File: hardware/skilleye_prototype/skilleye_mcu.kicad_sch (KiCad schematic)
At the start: 11 parts, among them SW1 SW_Push_45deg, SW2 SW_Push, U4 ESP32-C6-WROOM-1 (N8), U5 LSM6DS0

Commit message: added MCU schematic + datasheets
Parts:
- removed SW2: SW_Push, symbol Switch:SW_Push
- added C10: 0.1uF, symbol Device:C_Small
- added R10: 10K, symbol Device:R_Small
- added SW2: SW_Push_45deg, symbol Switch:SW_Push_45deg
- added TP1, TP2, TP3, TP4, TP5: TestPoint_Flag, symbol Connector:TestPoint_Flag
- C6: value 10uF -> 22uF
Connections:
- net +3V3: now also C9.1, R8.2, R9.2, U5.5 (VDDIO), U5.8 (VDD), C10.1, R10.2
- net GND: now also C9.2, U5.2 (SDIX), U5.3 (SCX), U5.6 (GND@6), U5.7 (GND@7), C10.2, SW2.2
- net at U4.10 (GPIO8): now also R8.1
- net at U4.11 (GPIO10): now also TP5.1
- net USB_DM: now reaches U4.13 (GPIO12/USB_D-)
- net USB_DP: now reaches U4.14 (GPIO13/USB_D+)
- net at U4.15 (GPIO9): now also R9.1, SW2.1
- net SPI_MOSI: now reaches U4.16 (GPIO18)
- net SPI_MOSI: now also U5.14 (SDA)
- net SPI_CLK: now reaches U4.17 (GPIO19)
- net SPI_CLK: now also U5.13 (SCL)
- net SPI_CS: now reaches U4.18 (GPIO20)
- net SPI_CS: now also U5.12 (~{CS}), R10.1
- net SPI_MISO: now reaches U4.19 (GPIO21)
- net SPI_MISO: now also U5.1 (SDO/SA0)
- net IMU_INT1: now reaches U4.20 (GPIO22)
- net IMU_INT1: now also U5.4 (INT1)
- net IMU_INT2: now reaches U4.21 (GPIO23)
- net IMU_INT2: now also U5.9 (INT2)
- net at U4.24 (U0RXD/GPIO17): now also TP2.1
- net at U4.25 (U0TXD/GPIO16): now also TP1.1
- net at U4.26 (GPIO3/ADC1_CH3): now also TP4.1
- net at U4.27 (GPIO2/ADC1_CH2): now also TP3.1
- no-connect marks 0 -> 10
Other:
- title: (none) -> MCU
- moved on the sheet: C6, C7, C8, C9, R7, R8, R9, SW1, U4, U5

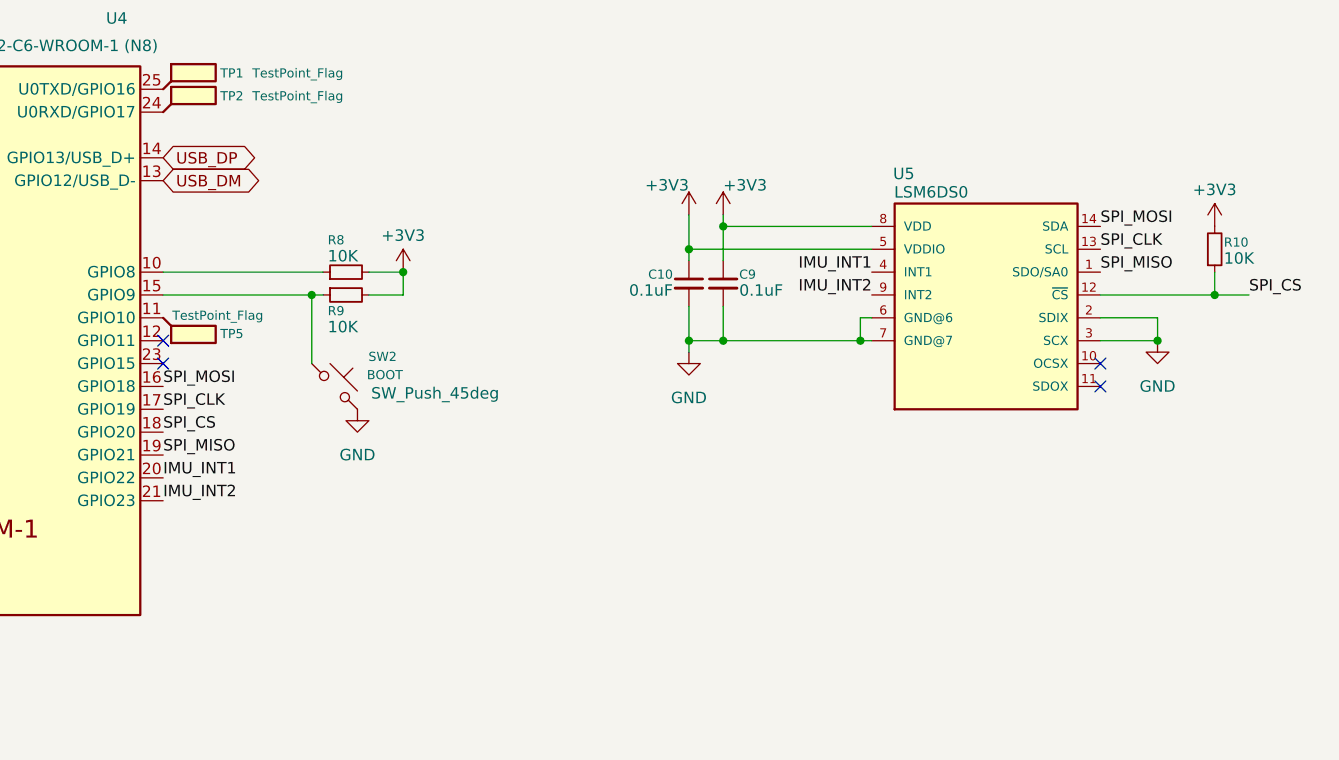
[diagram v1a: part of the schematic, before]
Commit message: prototype schematic rev1.1 - add VBUS sense divider
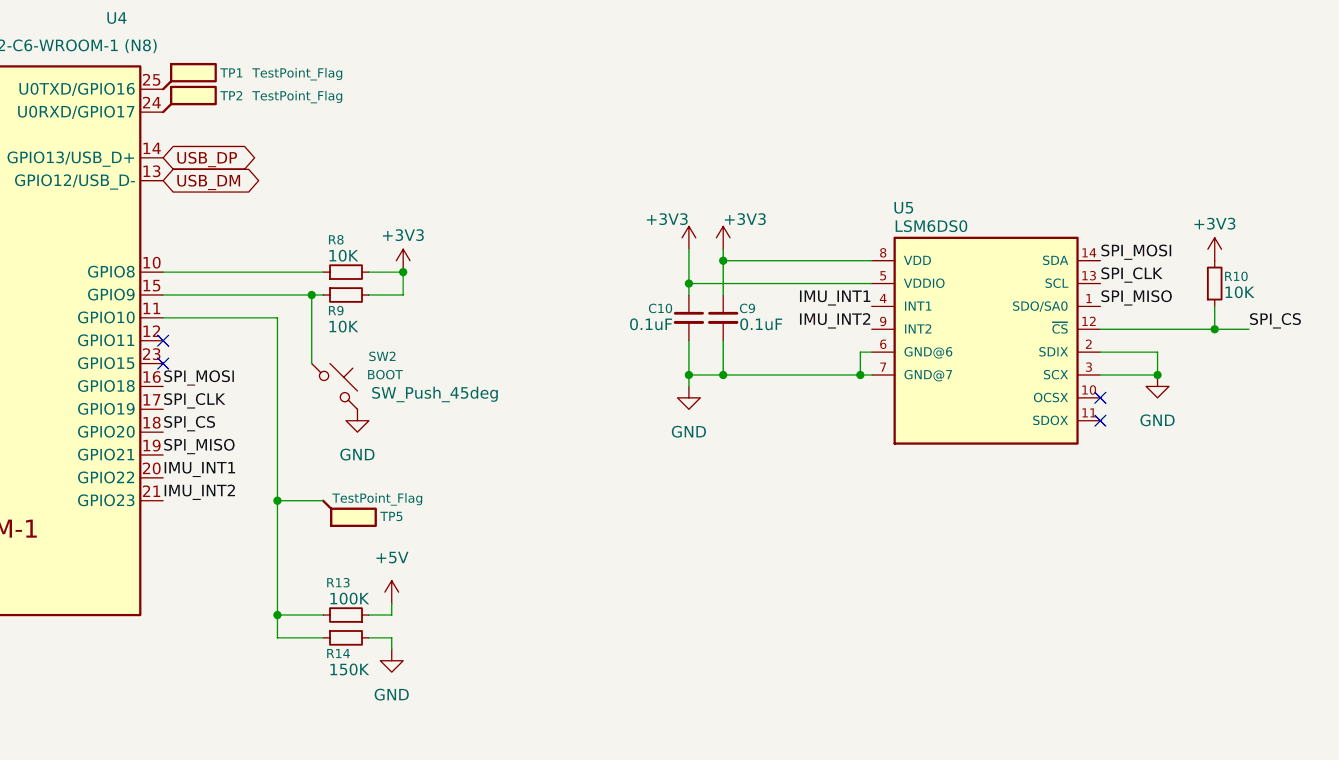
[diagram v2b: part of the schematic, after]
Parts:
- added R13: 100K, symbol Device:R_Small
- added R14: 150K, symbol Device:R_Small
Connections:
- net GND: now also R14.2
- net at TP5.1, U4.11 (GPIO10): now also R13.2, R14.1
- new net +5V: R13.1
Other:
- moved on the sheet: C10, C9, R10, TP5, U5
